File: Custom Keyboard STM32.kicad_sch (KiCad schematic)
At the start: 297 parts

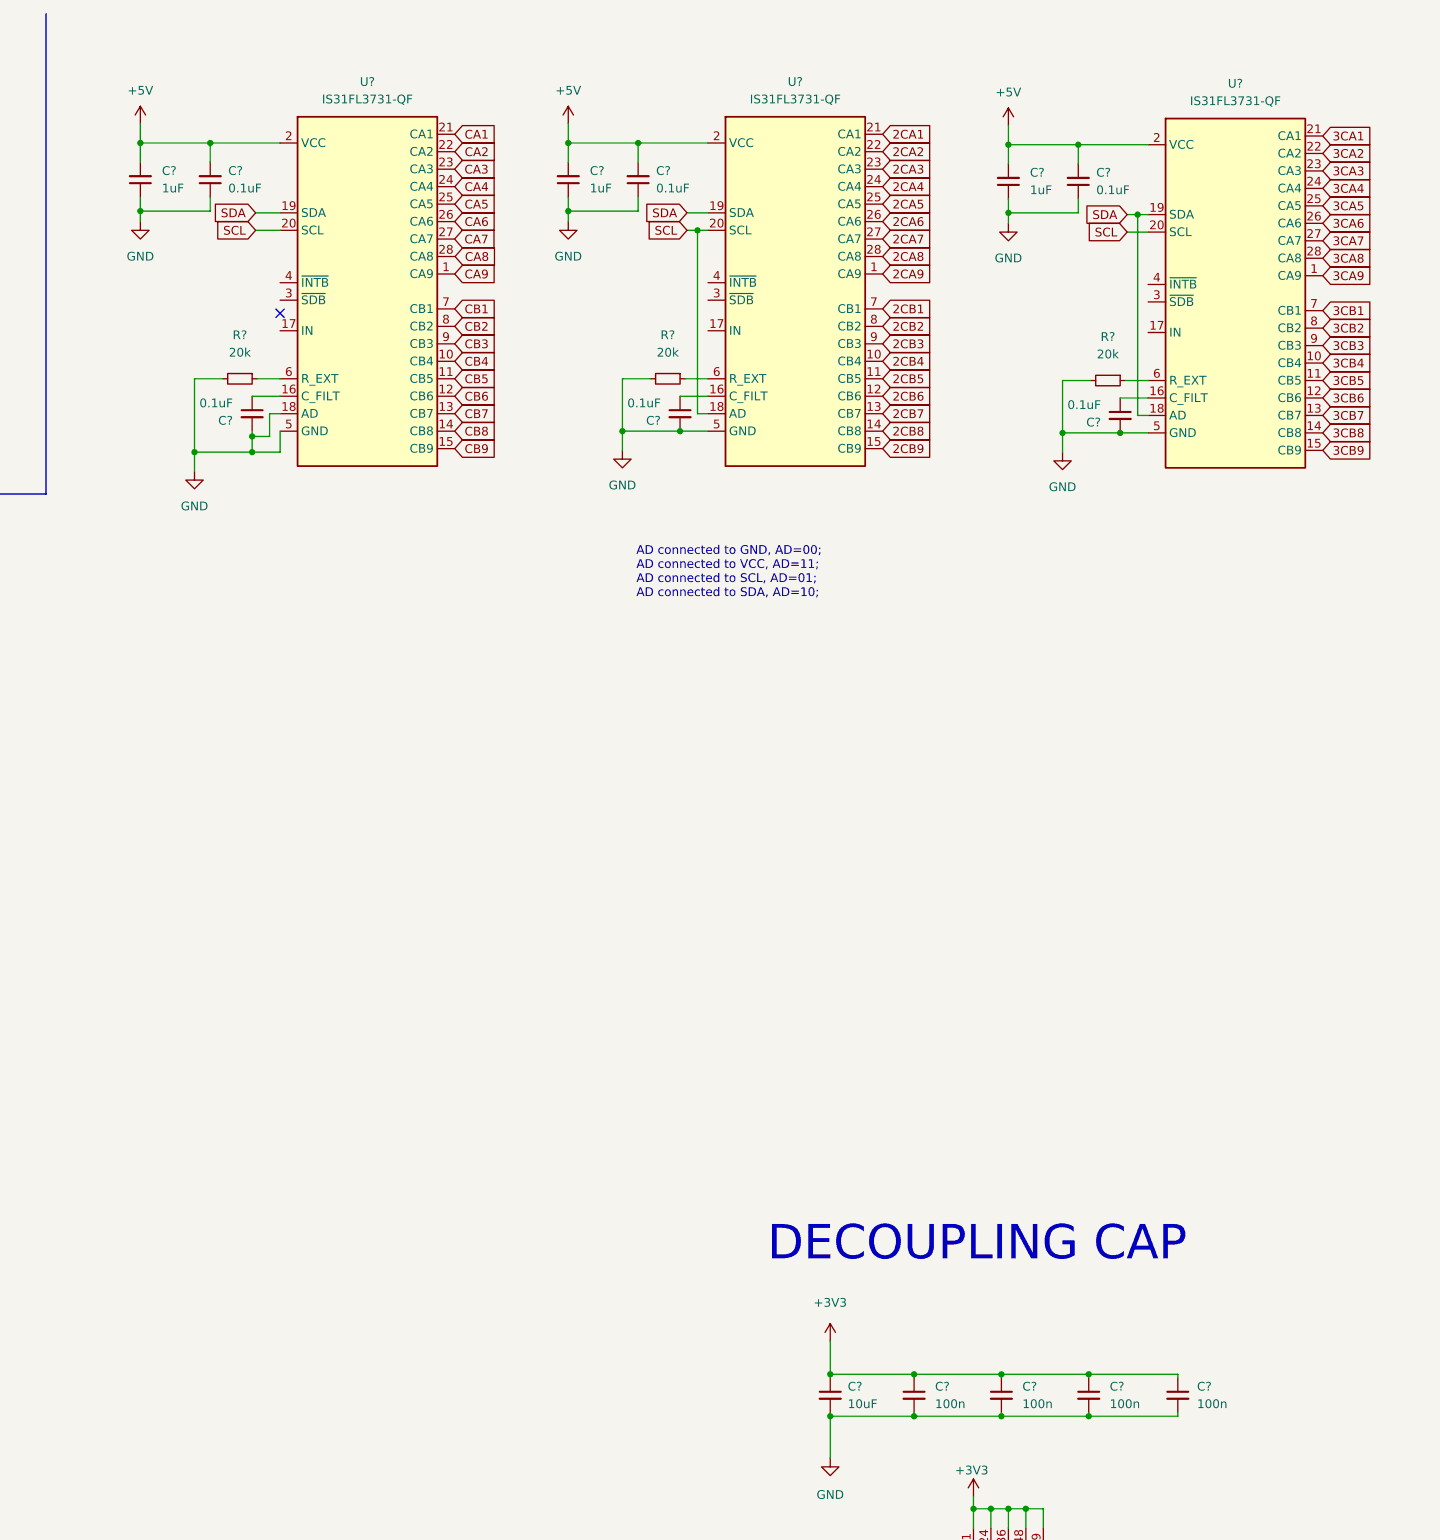
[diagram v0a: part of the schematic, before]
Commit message: Update Custom Keyboard STM32.kicad_sch
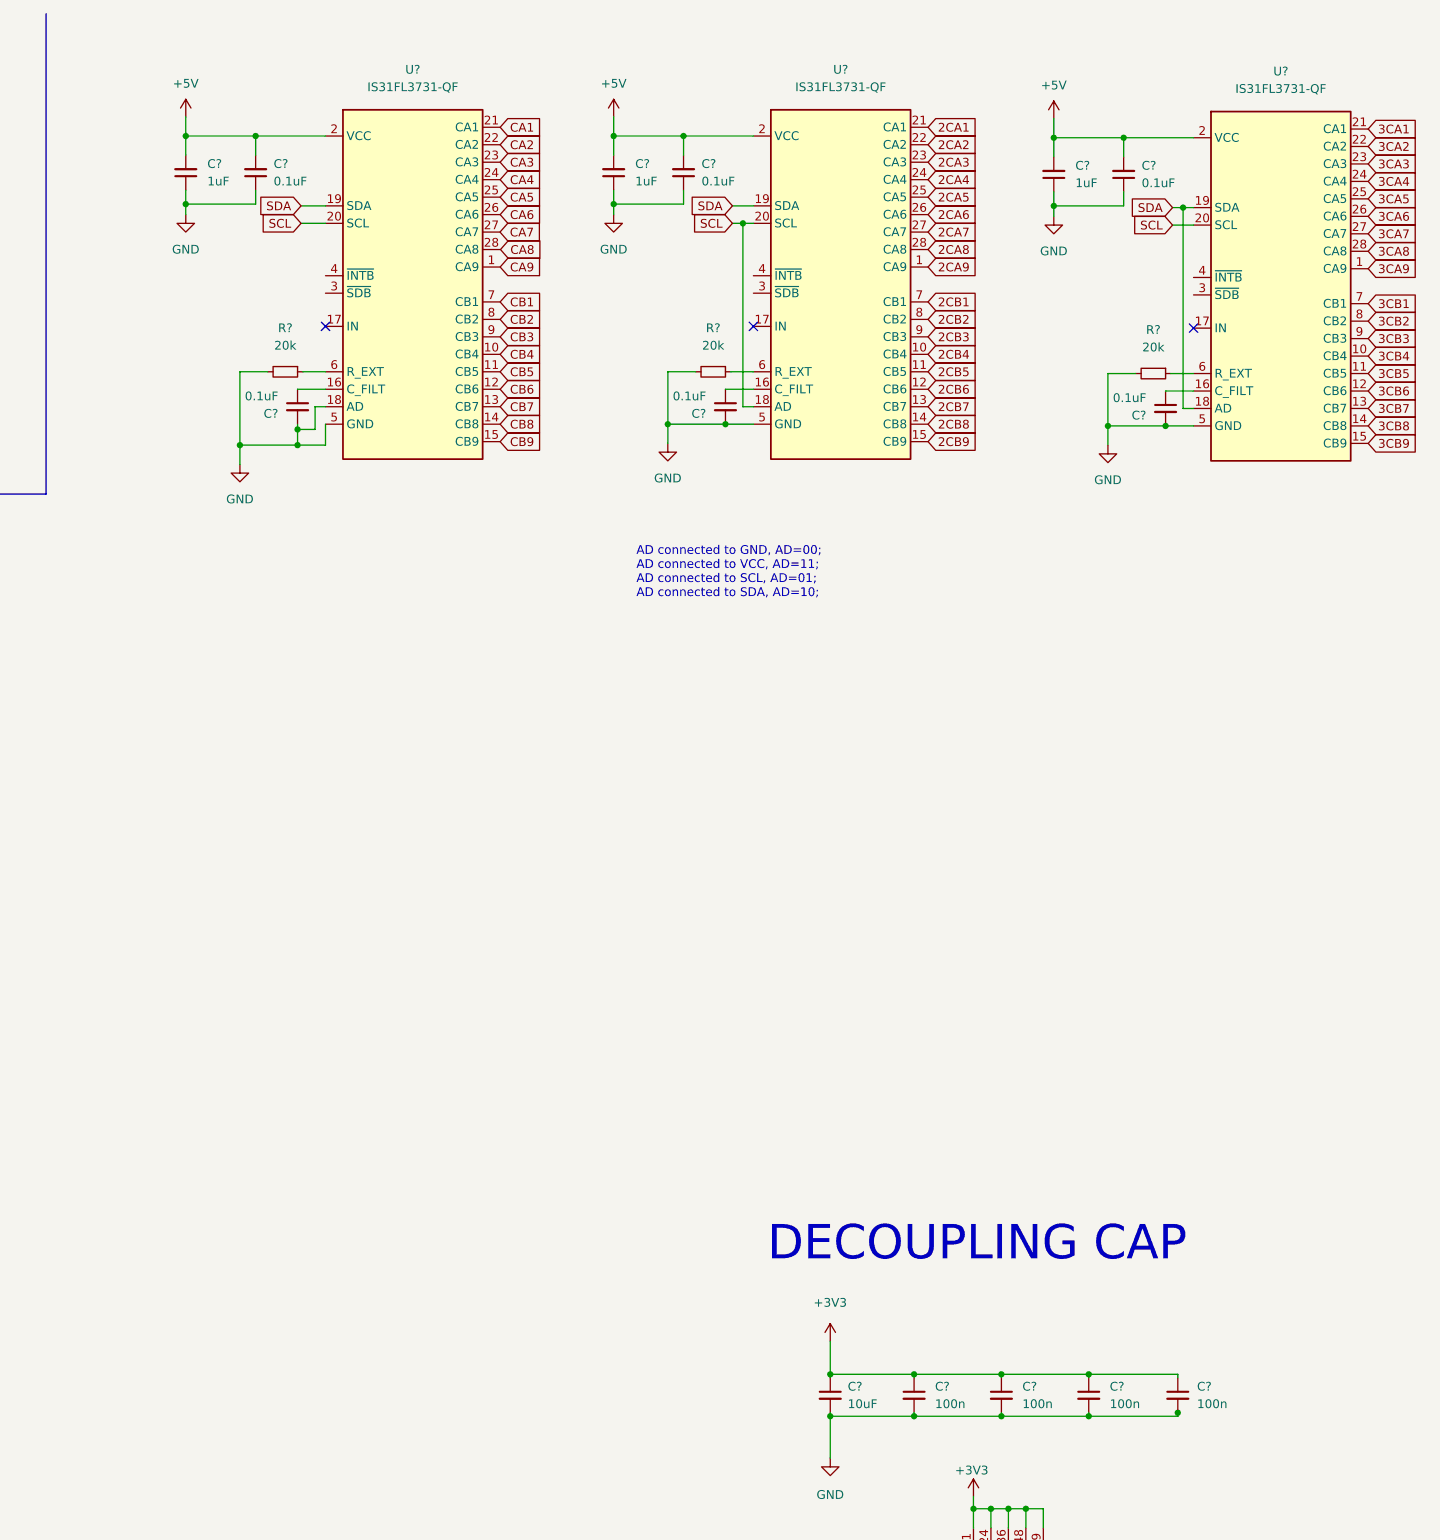
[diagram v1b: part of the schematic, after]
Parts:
- removed U? (x3): IS31FL3731-QF, Package_DFN_QFN:QFN-28-1EP_4x4mm_P0.4mm_EP2.3x2.3mm, symbol LEDDRIVER:IS31FL3731-QF
- added U? (x3): IS31FL3731-QF, Package_DFN_QFN:QFN-28-1EP_4x4mm_P0.4mm_EP2.3x2.3mm, symbol LEDDRIVER:IS31FL3731-QF
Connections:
- net +5V: now also U?.2 (VCC), U?.2 (VCC), U?.2 (VCC)
- net 2CA1: now also U?.21 (CA1)
- net 2CA2: now also U?.22 (CA2)
- net 2CA3: now also U?.23 (CA3)
- net 2CA4: now also U?.24 (CA4)
- net 2CA5: now also U?.25 (CA5)
- net 2CA6: now also U?.26 (CA6)
- net 2CA7: now also U?.27 (CA7)
- net 2CA8: now also U?.28 (CA8)
- net 2CA9: now also U?.1 (CA9)
- net 2CB1: now also U?.7 (CB1)
- net 2CB2: now also U?.8 (CB2)
- net 2CB3: now also U?.9 (CB3)
- net 2CB4: now also U?.10 (CB4)
- net 2CB5: now also U?.11 (CB5)
- net 2CB6: now also U?.12 (CB6)
- net 2CB7: now also U?.13 (CB7)
- net 2CB8: now also U?.14 (CB8)
- net 2CB9: now also U?.15 (CB9)
- net 3CA1: now also U?.21 (CA1)
- net 3CA2: now also U?.22 (CA2)
- net 3CA3: now also U?.23 (CA3)
- net 3CA4: now also U?.24 (CA4)
- net 3CA5: now also U?.25 (CA5)
- net 3CA6: now also U?.26 (CA6)
- net 3CA7: now also U?.27 (CA7)
- net 3CA8: now also U?.28 (CA8)
- net 3CA9: now also U?.1 (CA9)
- net 3CB1: now also U?.7 (CB1)
- net 3CB2: now also U?.8 (CB2)
- net 3CB3: now also U?.9 (CB3)
- net 3CB4: now also U?.10 (CB4)
- net 3CB5: now also U?.11 (CB5)
- net 3CB6: now also U?.12 (CB6)
- net 3CB7: now also U?.13 (CB7)
- net 3CB8: now also U?.14 (CB8)
- net 3CB9: now also U?.15 (CB9)
- net CA1: now also U?.21 (CA1)
- net CA2: now also U?.22 (CA2)
- net CA3: now also U?.23 (CA3)
- net CA4: now also U?.24 (CA4)
- net CA5: now also U?.25 (CA5)
- net CA6: now also U?.26 (CA6)
- net CA9: now also U?.1 (CA9)
- net CB1: now also U?.7 (CB1)
- net CB2: now also U?.8 (CB2)
- net CB3: now also U?.9 (CB3)
- net CB4: now also U?.10 (CB4)
- net CB5: now also U?.11 (CB5)
- net CB6: now also U?.12 (CB6)
- net CB7: now also U?.13 (CB7)
- net CB8: now also U?.14 (CB8)
- net CB9: now also U?.15 (CB9)
- net GND: now also U?.18 (AD), U?.29 (GND), U?.29 (GND), U?.29 (GND), U?.5 (GND), U?.5 (GND), U?.5 (GND)
- net SCL: now also U?.18 (AD), U?.20 (SCL), U?.20 (SCL), U?.20 (SCL)
- net SDA: now also U?.18 (AD), U?.19 (SDA), U?.19 (SDA), U?.19 (SDA)
- net at C?.1: now also U?.16 (C_FILT) (x3)
- net at R?.1: now also U?.6 (R_EXT) (x3)
- no-connect marks 3 -> 5
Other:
- moved on the sheet: C?, R?

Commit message: IS31FL3731
old led matrix
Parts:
- added U? (x2): IS31FL3733-TQ, Package_QFP:TQFP-48-1EP_7x7mm_P0.5mm_EP5x5mm, symbol Driver_LED:IS31FL3733-TQ
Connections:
- new net: U?.12 (PGND), U?.5 (PGND) (x2)
- new net: U?.48 (GND), U?.49 (GND) (x2)
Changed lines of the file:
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@@
     (pin "4")
   )
+  (symbol (lib_id "Driver_LED:IS31FL3733-TQ") (at 643.636 58.674 0) (unit 1)
+    (in_bom yes) (on_board yes) (fields_autoplaced)
+    (property "Reference" "U?" (id 0) (at 648.1954 99.06 0)
+      (effects (font (size 1.27 1.27)) (justify left))
+    )
+    (property "Value" "IS31FL3733-TQ" (id 1) (at 648.1954 101.6 0)
+      (effects (font (size 1.27 1.27)) (justify left))
+    )
+    (property "Footprint" "Package_QFP:TQFP-48-1EP_7x7mm_P0.5mm_EP5x5mm" (id 2) (at 643.636 58.674 0)
+      (effects (font (size 1.27 1.27)) hide)
+    )
+    (property "Datasheet" "http://www.issi.com/WW/pdf/IS31FL3733.pdf" (id 3) (at 643.636 58.674 0)
+      (effects (font (size 1.27 1.27)) hide)
+    )
+    (pin "1")
+    (pin "10")
+    (pin "11")
+    (pin "12")
+    (pin "13")
+    (pin "14")
+    (pin "15")
+    (pin "16")
+    (pin "17")
+    (pin "18")
+    (pin "19")
+    (pin "2")
+    (pin "20")
+    (pin "21")
+    (pin "22")
+    (pin "23")
+    (pin "24")
+    (pin "25")
+    (pin "26")
+    (pin "27")
+    (pin "28")
+    (pin "29")
+    (pin "3")
+    (pin "30")
+    (pin "31")
+    (pin "32")
+    (pin "33")
+    (pin "34")
+    (pin "35")
+    (pin "36")
+    (pin "37")
+    (pin "38")
+    (pin "39")
+    (pin "4")
+    (pin "40")
+    (pin "41")
+    (pin "42")
+    (pin "43")
+    (pin "44")
+    (pin "45")
+    (pin "46")
+    (pin "47")
+    (pin "48")
+    (pin "49")
+    (pin "5")
+    (pin "6")
+    (pin "7")
+    (pin "8")
+    (pin "9")
+  )
   (symbol (lib_id "Device:LED_ARGB") (at 169.926 351.79 0) (mirror x) (unit 1)
     (in_bom yes) (on_board yes) (fields_autoplaced)
@@
     (pin "4")
   )
+  (symbol (lib_id "Driver_LED:IS31FL3733-TQ") (at 719.7544 58.674 0) (unit 1)
+    (in_bom yes) (on_board yes) (fields_autoplaced)
+    (property "Reference" "U?" (id 0) (at 724.3138 99.06 0)
+      (effects (font (size 1.27 1.27)) (justify left))
+    )
+    (property "Value" "IS31FL3733-TQ" (id 1) (at 724.3138 101.6 0)
+      (effects (font (size 1.27 1.27)) (justify left))
+    )
+    (property "Footprint" "Package_QFP:TQFP-48-1EP_7x7mm_P0.5mm_EP5x5mm" (id 2) (at 719.7544 58.674 0)
+      (effects (font (size 1.27 1.27)) hide)
+    )
+    (property "Datasheet" "http://www.issi.com/WW/pdf/IS31FL3733.pdf" (id 3) (at 719.7544 58.674 0)
+      (effects (font (size 1.27 1.27)) hide)
+    )
+    (pin "1")
+    (pin "10")
+    (pin "11")
+    (pin "12")
+    (pin "13")
+    (pin "14")
+    (pin "15")
+    (pin "16")
+    (pin "17")
+    (pin "18")
+    (pin "19")
+    (pin "2")
+    (pin "20")
+    (pin "21")
+    (pin "22")
+    (pin "23")
+    (pin "24")
+    (pin "25")
+    (pin "26")
+    (pin "27")
+    (pin "28")
+    (pin "29")
+    (pin "3")
+    (pin "30")
+    (pin "31")
+    (pin "32")
+    (pin "33")
+    (pin "34")
+    (pin "35")
+    (pin "36")
+    (pin "37")
+    (pin "38")
+    (pin "39")
+    (pin "4")
+    (pin "40")
+    (pin "41")
+    (pin "42")
+    (pin "43")
+    (pin "44")
+    (pin "45")
+    (pin "46")
+    (pin "47")
+    (pin "48")
+    (pin "49")
+    (pin "5")
+    (pin "6")
+    (pin "7")
+    (pin "8")
+    (pin "9")
+  )
   (symbol (lib_id "MX_Alps_Hybrid:MX-NoLED") (at 208.28 58.928 0) (unit 1)
     (in_bom yes) (on_board yes) (fields_autoplaced)
@@
       (reference "U?") (unit 1) (value "IS31FL3731-QF") (footprint "Package_DFN_QFN:QFN-28-1EP_4x4mm_P0.4mm_EP2.3x2.3mm")
     )
+    (path "/a60815e1-7af7-426a-845b-ae3ab009be78"
+      (reference "U?") (unit 1) (value "IS31FL3733-TQ") (footprint "Package_QFP:TQFP-48-1EP_7x7mm_P0.5mm_EP5x5mm")
+    )
+    (path "/c8a38c6d-7395-4674-ac4a-836e2b764d6e"
+      (reference "U?") (unit 1) (value "IS31FL3733-TQ") (footprint "Package_QFP:TQFP-48-1EP_7x7mm_P0.5mm_EP5x5mm")
+    )
     (path "/ca2ab5db-c1d7-43e6-a748-730afb270859"

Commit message: new reset circuit
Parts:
- removed C?: C_Small, symbol Device:C_Small
- removed C? (x6): 0.1uF, symbol Device:C_Small
- removed C? (x3): 1uF, symbol Device:C_Small
- removed D? (x87): LED_ARGB, symbol Device:LED_ARGB
- removed J?: USB_C_Receptacle, symbol Connector:USB_C_Receptacle
- removed R? (x3): 20k, symbol Device:R_Small
- removed R? (x2): 4.7k, symbol Device:R_Small
- removed R?: R_Small, symbol Device:R_Small
- removed SW?: SW_Push, symbol Switch:SW_Push
- removed U? (x3): IS31FL3731-QF, Package_DFN_QFN:QFN-28-1EP_4x4mm_P0.4mm_EP2.3x2.3mm, symbol LEDDRIVER:IS31FL3731-QF
- added C? (x8): 0.47uF, symbol BgrA:C_Small
- added C? (x6): 0.1uF, symbol BgrA:C_Small
- added C?: 4.7uF, symbol BgrA:C_Small
- added C?: 100k, symbol BgrA:C_Small
- added C?: 1uF, symbol BgrA:C_Small
- added D? (x95): LED_ABGR, symbol BgrA:LED_ABGR
- added F?: Polyfuse_Small, symbol BgrA:Polyfuse_Small
- added Q?: 2N7002, Package_TO_SOT_SMD:SOT-23, symbol Transistor_FET:2N7002
- added R? (x3): 100k, symbol BgrA:R_Small
- added R? (x2): 10k, symbol BgrA:R_Small
- added R? (x2): 20k, symbol BgrA:R_Small
- added R? (x2): 2k, symbol BgrA:R_Small
- added SW?: SW_Push, symbol Switch:SW_Push
- C?: value 22pF -> 20pF
- C?: value C_SMALL -> 20pF
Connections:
- net +3V3: now also C?.2, R?.1, R?.1, R?.1, SW?.2
- net +5V: now also U?.20 (PVCC), U?.20 (PVCC), U?.29 (PVCC), U?.29 (PVCC), U?.37 (AVCC), U?.37 (AVCC), U?.38 (DVCC), U?.38 (DVCC), U?.39 (VIO), U?.39 (VIO), U?.43 (ADDR1), C?.1, C?.1, C?.1, C?.1, C?.1, C?.1, C?.1, C?.1, C?.1, C?.1, C?.1, C?.1, C?.1, C?.1
- net BOOT0: now also C?.1, R?.1, SW?.1
- net GND: now also U?.12 (PGND), U?.12 (PGND), U?.34 (AGND), U?.34 (AGND), U?.43 (ADDR1), U?.44 (ADDR2), U?.44 (ADDR2), U?.48 (GND), U?.48 (GND), U?.49 (GND), U?.49 (GND), U?.5 (PGND), U?.5 (PGND), C?.2, C?.2, C?.2, C?.2, C?.2, C?.2, C?.2, C?.2, C?.2, C?.2, C?.2, C?.2, C?.2, C?.2, C?.2, C?.2, Q?.2 (S), R?.2, R?.2, R?.2, R?.2, R?.2, R?.2
- net NRST: now also C?.1, Q?.3 (D), R?.2
- net SCL: now also U?.42 (SCL), U?.42 (SCL), R?.2
- net SDA: now also U?.41 (SDA), U?.41 (SDA), R?.2
- net SDB: now reaches U?.34 (PA13)
- net SDB: now also U?.46 (~{SDB}), U?.46 (~{SDB}), C?.1
- net SW8: now reaches U?.10 (SW8)
- net SW8: now also D?.4 (RK), D?.4 (RK), D?.4 (RK), D?.4 (RK), D?.4 (RK), D?.4 (RK), D?.4 (RK), D?.4 (RK), D?.4 (RK), D?.4 (RK), D?.4 (RK), D?.4 (RK), D?.4 (RK), D?.4 (RK), D?.4 (RK), D?.4 (RK)
- net SW9: now reaches U?.11 (SW9)
- net SW9: now also D?.2 (BK), D?.2 (BK), D?.2 (BK), D?.2 (BK), D?.2 (BK), D?.2 (BK), D?.2 (BK), D?.2 (BK), D?.2 (BK), D?.2 (BK), D?.2 (BK), D?.2 (BK), D?.2 (BK), D?.2 (BK), D?.2 (BK), D?.2 (BK)
- net SW10: now reaches U?.13 (SW10)
- net SW10: now also D?.3 (GK), D?.3 (GK), D?.3 (GK), D?.3 (GK), D?.3 (GK), D?.3 (GK), D?.3 (GK), D?.3 (GK), D?.3 (GK), D?.3 (GK), D?.3 (GK), D?.3 (GK), D?.3 (GK), D?.3 (GK), D?.3 (GK), D?.3 (GK)
- net SW11: now reaches U?.14 (SW11)
- net SW11: now also D?.4 (RK), D?.4 (RK), D?.4 (RK), D?.4 (RK), D?.4 (RK), D?.4 (RK), D?.4 (RK), D?.4 (RK), D?.4 (RK), D?.4 (RK), D?.4 (RK), D?.4 (RK), D?.4 (RK), D?.4 (RK), D?.4 (RK), D?.4 (RK)
- net SW12: now reaches U?.15 (SW12)
- net SW12: now also D?.2 (BK), D?.2 (BK), D?.2 (BK), D?.2 (BK), D?.2 (BK), D?.2 (BK), D?.2 (BK), D?.2 (BK), D?.2 (BK), D?.2 (BK), D?.2 (BK), D?.2 (BK), D?.2 (BK), D?.2 (BK), D?.2 (BK), D?.2 (BK)
- net CS1: now reaches U?.16 (CS1)
- net CS1: now also D?.1 (A), D?.1 (A), D?.1 (A), D?.1 (A)
- net CS2: now reaches U?.17 (CS2)
- net CS2: now also D?.1 (A), D?.1 (A), D?.1 (A), D?.1 (A)
- net CS3: now reaches U?.18 (CS3)
- net CS3: now also D?.1 (A), D?.1 (A), D?.1 (A), D?.1 (A)
- net CS4: now reaches U?.19 (CS4)
- net CS4: now also D?.1 (A), D?.1 (A), D?.1 (A), D?.1 (A)
- net SW1: now reaches U?.2 (SW1)
- net SW1: now also D?.3 (GK), D?.3 (GK), D?.3 (GK), D?.3 (GK), D?.3 (GK), D?.3 (GK), D?.3 (GK), D?.3 (GK), D?.3 (GK), D?.3 (GK), D?.3 (GK), D?.3 (GK), D?.3 (GK), D?.3 (GK), D?.3 (GK), D?.3 (GK)
- net CS5: now reaches U?.21 (CS5)
- net CS5: now also D?.1 (A), D?.1 (A), D?.1 (A), D?.1 (A)
- net CS6: now reaches U?.22 (CS6)
- net CS6: now also D?.1 (A), D?.1 (A), D?.1 (A), D?.1 (A)
- net CS7: now reaches U?.23 (CS7)
- net CS7: now also D?.1 (A), D?.1 (A), D?.1 (A), D?.1 (A)
- net CS8: now reaches U?.24 (CS8)
- net CS8: now also D?.1 (A), D?.1 (A), D?.1 (A), D?.1 (A)
- net CS9: now reaches U?.25 (CS9)
- net CS9: now also D?.1 (A), D?.1 (A), D?.1 (A), D?.1 (A)
- net CS10: now reaches U?.26 (CS10)
- net CS10: now also D?.1 (A), D?.1 (A), D?.1 (A), D?.1 (A)
- net CS11: now reaches U?.27 (CS11)
- net CS11: now also D?.1 (A), D?.1 (A), D?.1 (A), D?.1 (A)
- net CS12: now reaches U?.28 (CS12)
- net CS12: now also D?.1 (A), D?.1 (A), D?.1 (A), D?.1 (A)
- net SW2: now reaches U?.3 (SW2)
- net SW2: now also D?.4 (RK), D?.4 (RK), D?.4 (RK), D?.4 (RK), D?.4 (RK), D?.4 (RK), D?.4 (RK), D?.4 (RK), D?.4 (RK), D?.4 (RK), D?.4 (RK), D?.4 (RK), D?.4 (RK), D?.4 (RK), D?.4 (RK), D?.4 (RK)
- net CS13: now reaches U?.30 (CS13)
- net CS13: now also D?.1 (A), D?.1 (A), D?.1 (A), D?.1 (A)
- net CS14: now reaches U?.31 (CS14)
- net CS14: now also D?.1 (A), D?.1 (A), D?.1 (A), D?.1 (A)
- net CS15: now reaches U?.32 (CS15)
- net CS15: now also D?.1 (A), D?.1 (A), D?.1 (A), D?.1 (A)
- net CS16: now reaches U?.33 (CS16)
- net CS16: now also D?.1 (A), D?.1 (A), D?.1 (A), D?.1 (A)
- net at U?.35 (RSET): now also R?.1 (x2)
- net SW3: now reaches U?.4 (SW3)
- net SW3: now also D?.2 (BK), D?.2 (BK), D?.2 (BK), D?.2 (BK), D?.2 (BK), D?.2 (BK), D?.2 (BK), D?.2 (BK), D?.2 (BK), D?.2 (BK), D?.2 (BK), D?.2 (BK), D?.2 (BK), D?.2 (BK), D?.2 (BK), D?.2 (BK)
- net SYNC: now reaches U?.40 (SYNC)
- net SYNC: now also U?.40 (SYNC)
- net at U?.47 (IICRST): now also R?.1 (x2)
- net SW4: now reaches U?.6 (SW4)
- net SW4: now also D?.3 (GK), D?.3 (GK), D?.3 (GK), D?.3 (GK), D?.3 (GK), D?.3 (GK), D?.3 (GK), D?.3 (GK), D?.3 (GK), D?.3 (GK), D?.3 (GK), D?.3 (GK), D?.3 (GK), D?.3 (GK), D?.3 (GK), D?.3 (GK)
- net SW5: now reaches U?.7 (SW5)
- net SW5: now also D?.4 (RK), D?.4 (RK), D?.4 (RK), D?.4 (RK), D?.4 (RK), D?.4 (RK), D?.4 (RK), D?.4 (RK), D?.4 (RK), D?.4 (RK), D?.4 (RK), D?.4 (RK), D?.4 (RK), D?.4 (RK), D?.4 (RK), D?.4 (RK)
- net SW6: now reaches U?.8 (SW6)
- net SW6: now also D?.2 (BK), D?.2 (BK), D?.2 (BK), D?.2 (BK), D?.2 (BK), D?.2 (BK), D?.2 (BK), D?.2 (BK), D?.2 (BK), D?.2 (BK), D?.2 (BK), D?.2 (BK), D?.2 (BK), D?.2 (BK), D?.2 (BK), D?.2 (BK)
- net SW7: now reaches U?.9 (SW7)
- net SW7: now also D?.3 (GK), D?.3 (GK), D?.3 (GK), D?.3 (GK), D?.3 (GK), D?.3 (GK), D?.3 (GK), D?.3 (GK), D?.3 (GK), D?.3 (GK), D?.3 (GK), D?.3 (GK), D?.3 (GK), D?.3 (GK), D?.3 (GK), D?.3 (GK)
- net ACS1: now reaches U?.16 (CS1)
- net ACS1: now also D?.1 (A), D?.1 (A)
- net ACS2: now reaches U?.17 (CS2)
- net ACS2: now also D?.1 (A), D?.1 (A)
- net ACS3: now reaches U?.18 (CS3)
- net ACS3: now also D?.1 (A), D?.1 (A)
- net ACS4: now reaches U?.19 (CS4)
- net ACS4: now also D?.1 (A), D?.1 (A)
- net ASW1: now reaches U?.2 (SW1)
- net ASW1: now also D?.3 (GK), D?.3 (GK), D?.3 (GK), D?.3 (GK), D?.3 (GK), D?.3 (GK), D?.3 (GK), D?.3 (GK), D?.3 (GK), D?.3 (GK), D?.3 (GK), D?.3 (GK), D?.3 (GK), D?.3 (GK), D?.3 (GK), D?.3 (GK)
- net ACS5: now reaches U?.21 (CS5)
- net ACS5: now also D?.1 (A), D?.1 (A)
- net ACS6: now reaches U?.22 (CS6)
- net ACS6: now also D?.1 (A), D?.1 (A)
- net ACS7: now reaches U?.23 (CS7)
- net ACS7: now also D?.1 (A), D?.1 (A)
- net ACS8: now reaches U?.24 (CS8)
- net ACS8: now also D?.1 (A), D?.1 (A)
- net ACS9: now reaches U?.25 (CS9)
- net ACS9: now also D?.1 (A), D?.1 (A)
- net ACS10: now reaches U?.26 (CS10)
- net ACS10: now also D?.1 (A), D?.1 (A)
- net ACS11: now reaches U?.27 (CS11)
- net ACS11: now also D?.1 (A), D?.1 (A)
- net ACS12: now reaches U?.28 (CS12)
- net ACS12: now also D?.1 (A), D?.1 (A)
- net ASW2: now reaches U?.3 (SW2)
- net ASW2: now also D?.4 (RK), D?.4 (RK), D?.4 (RK), D?.4 (RK), D?.4 (RK), D?.4 (RK), D?.4 (RK), D?.4 (RK), D?.4 (RK), D?.4 (RK), D?.4 (RK), D?.4 (RK), D?.4 (RK), D?.4 (RK), D?.4 (RK), D?.4 (RK)
- net ACS13: now reaches U?.30 (CS13)
- net ACS13: now also D?.1 (A), D?.1 (A)
- net ACS14: now reaches U?.31 (CS14)
- net ACS14: now also D?.1 (A), D?.1 (A)
- net ACS15: now reaches U?.32 (CS15)
- net ACS15: now also D?.1 (A), D?.1 (A)
- net ACS16: now reaches U?.33 (CS16)
- net ACS16: now also D?.1 (A)
- net ASW3: now reaches U?.4 (SW3)
- net ASW3: now also D?.2 (BK), D?.2 (BK), D?.2 (BK), D?.2 (BK), D?.2 (BK), D?.2 (BK), D?.2 (BK), D?.2 (BK), D?.2 (BK), D?.2 (BK), D?.2 (BK), D?.2 (BK), D?.2 (BK), D?.2 (BK), D?.2 (BK), D?.2 (BK)
- net ASW4: now reaches U?.6 (SW4)
- net ASW4: now also D?.3 (GK), D?.3 (GK), D?.3 (GK), D?.3 (GK), D?.3 (GK), D?.3 (GK), D?.3 (GK), D?.3 (GK), D?.3 (GK), D?.3 (GK), D?.3 (GK), D?.3 (GK), D?.3 (GK), D?.3 (GK), D?.3 (GK)
- net ASW5: now reaches U?.7 (SW5)
- net ASW5: now also D?.4 (RK), D?.4 (RK), D?.4 (RK), D?.4 (RK), D?.4 (RK), D?.4 (RK), D?.4 (RK), D?.4 (RK), D?.4 (RK), D?.4 (RK), D?.4 (RK), D?.4 (RK), D?.4 (RK), D?.4 (RK), D?.4 (RK)
- net ASW6: now reaches U?.8 (SW6)
- net ASW6: now also D?.2 (BK), D?.2 (BK), D?.2 (BK), D?.2 (BK), D?.2 (BK), D?.2 (BK), D?.2 (BK), D?.2 (BK), D?.2 (BK), D?.2 (BK), D?.2 (BK), D?.2 (BK), D?.2 (BK), D?.2 (BK), D?.2 (BK)
- net 5V: no longer names the net of C?.2, U?.3 (VI)
- net 5V: now also F?.2; no longer USB?.11 (VBUS), USB?.2 (VBUS)
- new net: C?.2, Q?.1 (G), R?.1
- new net VBUS: F?.1, USB?.11 (VBUS), USB?.2 (VBUS)
- no-connect marks 5 -> 10
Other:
- moved on the sheet: C?, U?
